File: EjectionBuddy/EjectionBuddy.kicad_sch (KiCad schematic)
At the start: 19 parts, among them J2 Conn_01x08, SW1 SW_Push, SW2 SW_Push, U1 ESP32-S3-MINI-1

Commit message: More work on the side-mcu, ongoing
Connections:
- net EN: now reaches C7.1, R21.2, SW1.2, U1.45 (EN)
- net 0: now reaches C9.1, SW2.2, U1.4 (IO0)
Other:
- sheet connector renamed connecter
- added sheet side_mcu (side_mcu.kicad_sch)
- sheet connecter: file connector.kicad_sch -> connecter.kicad_sch
- note added: "MCUs"
- note removed: "MCU"
- moved on the sheet: C1, C2, C7, C9, D10, D12, D13, D14, D15, R21, R22, R23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

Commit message: Finished! QR and instruction pending
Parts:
- removed C1: 10u, Capacitor_SMD:C_0603_1608Metric, symbol Device:C
- removed C2, C7, C9: 0.1u, Capacitor_SMD:C_0603_1608Metric, symbol Device:C
- removed D10, D12, D13, D14, D15: LED, symbol Device:LED
- removed J2: Conn_01x08, symbol Connector_Generic:Conn_01x08
- removed R21: 10k, Resistor_SMD:R_0603_1608Metric, symbol Device:R
- removed R22, R23, R24: 39k, symbol Device:R
- removed R26: 1k, symbol Device:R
- removed R27: 2.7k, symbol Device:R
- removed SW1, SW2: SW_Push, Button_Switch_SMD:SW_SPST_PTS810, symbol Switch:SW_Push
- removed U1: ESP32-S3-MINI-1, RF_Module:ESP32-S2-MINI-1, symbol RF_Module:ESP32-S3-MINI-1
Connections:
- no-connect marks 16 -> 0
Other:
- sheet sense renamed power_sense
- added sheet baro (baro.kicad_sch)
- added sheet detach_sense (detach_sense.kicad_sch)
- added sheet imu (imu.kicad_sch)
- added sheet led (led.kicad_sch)
- added sheet main_mcu (main_mcu.kicad_sch)
- added sheet stamp (stamp.kicad_sch)
- sheet connecter ports: added SM{SERIAL}, SM{SWD}; removed none
- sheet power_sense: file sense.kicad_sch -> power_sense.kicad_sch
- sheet side_mcu ports: added ONEWIRE, {SERIAL}, {SWD}; removed none
- sheet usb ports: added {USB}; removed D+, D-
- note added: "2025/4/3 - 4/13"
- note added: "SW_VBATOUT pull low to cut SW_PWRCUT pull high to cut"
- note added: "Sensors"
- note added: "v0.1"
- note removed: "0, 3, 45, 46 are strapping pins. 47, 48 work at 1.8V."
- note removed: "2025/4/3"
- note removed: "Breakouts in pads"
- note removed: "Green"
- note removed: "MCU module"
- note removed: "Red"

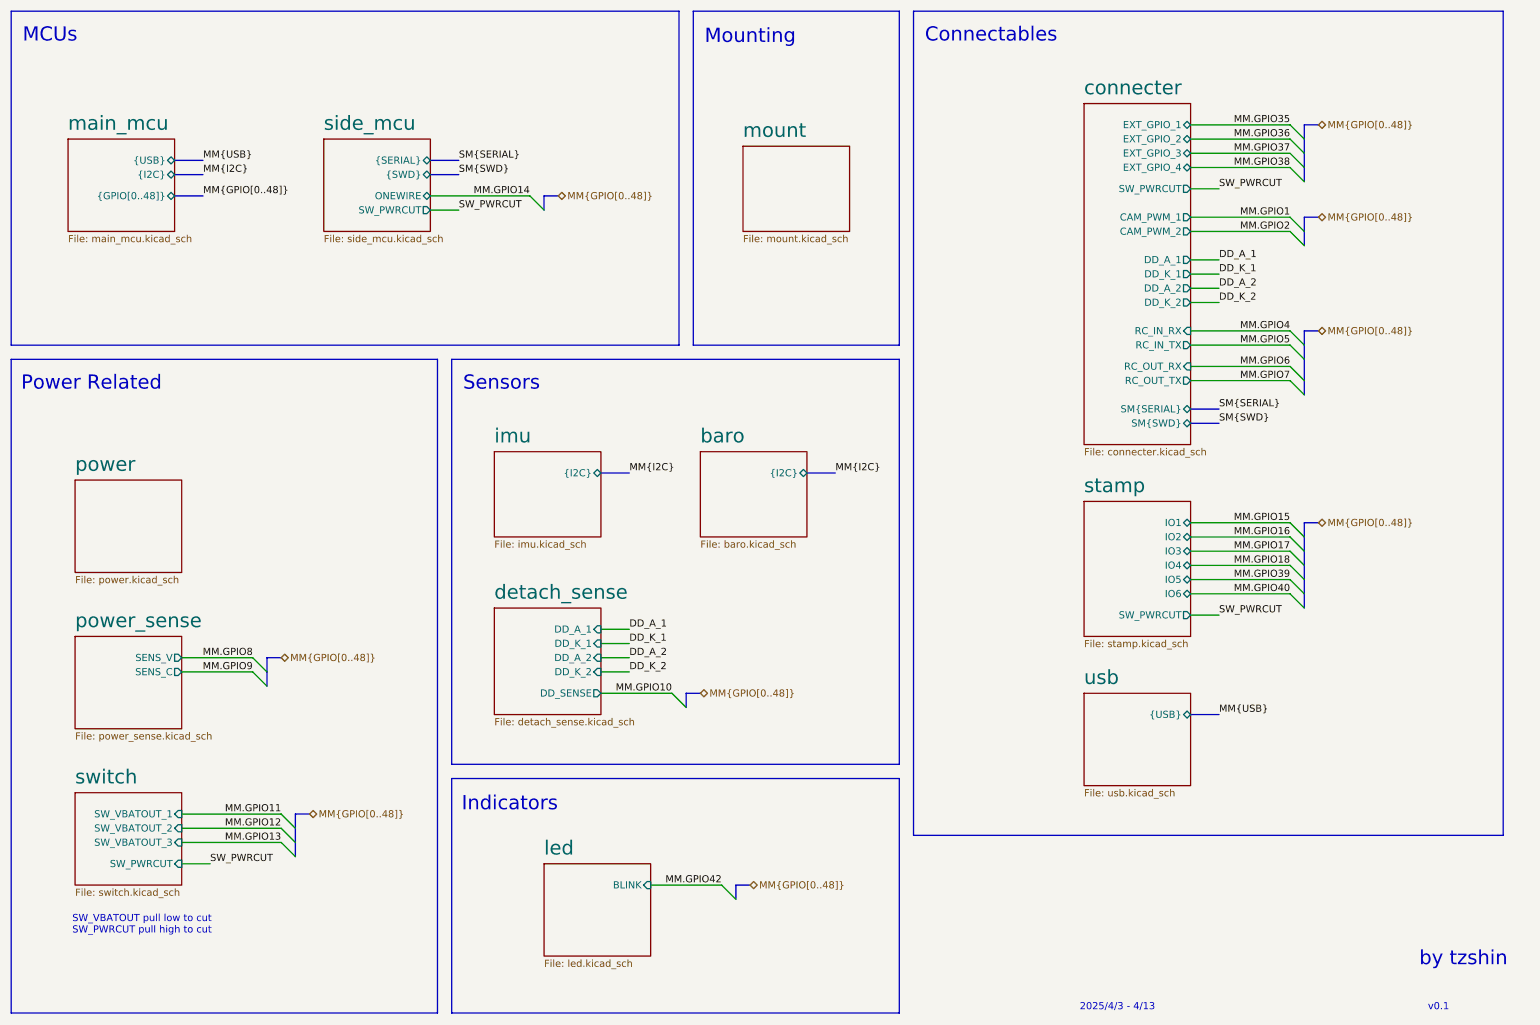
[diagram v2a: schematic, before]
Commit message: Side-mcu stm -> attiny, with improvements here and there
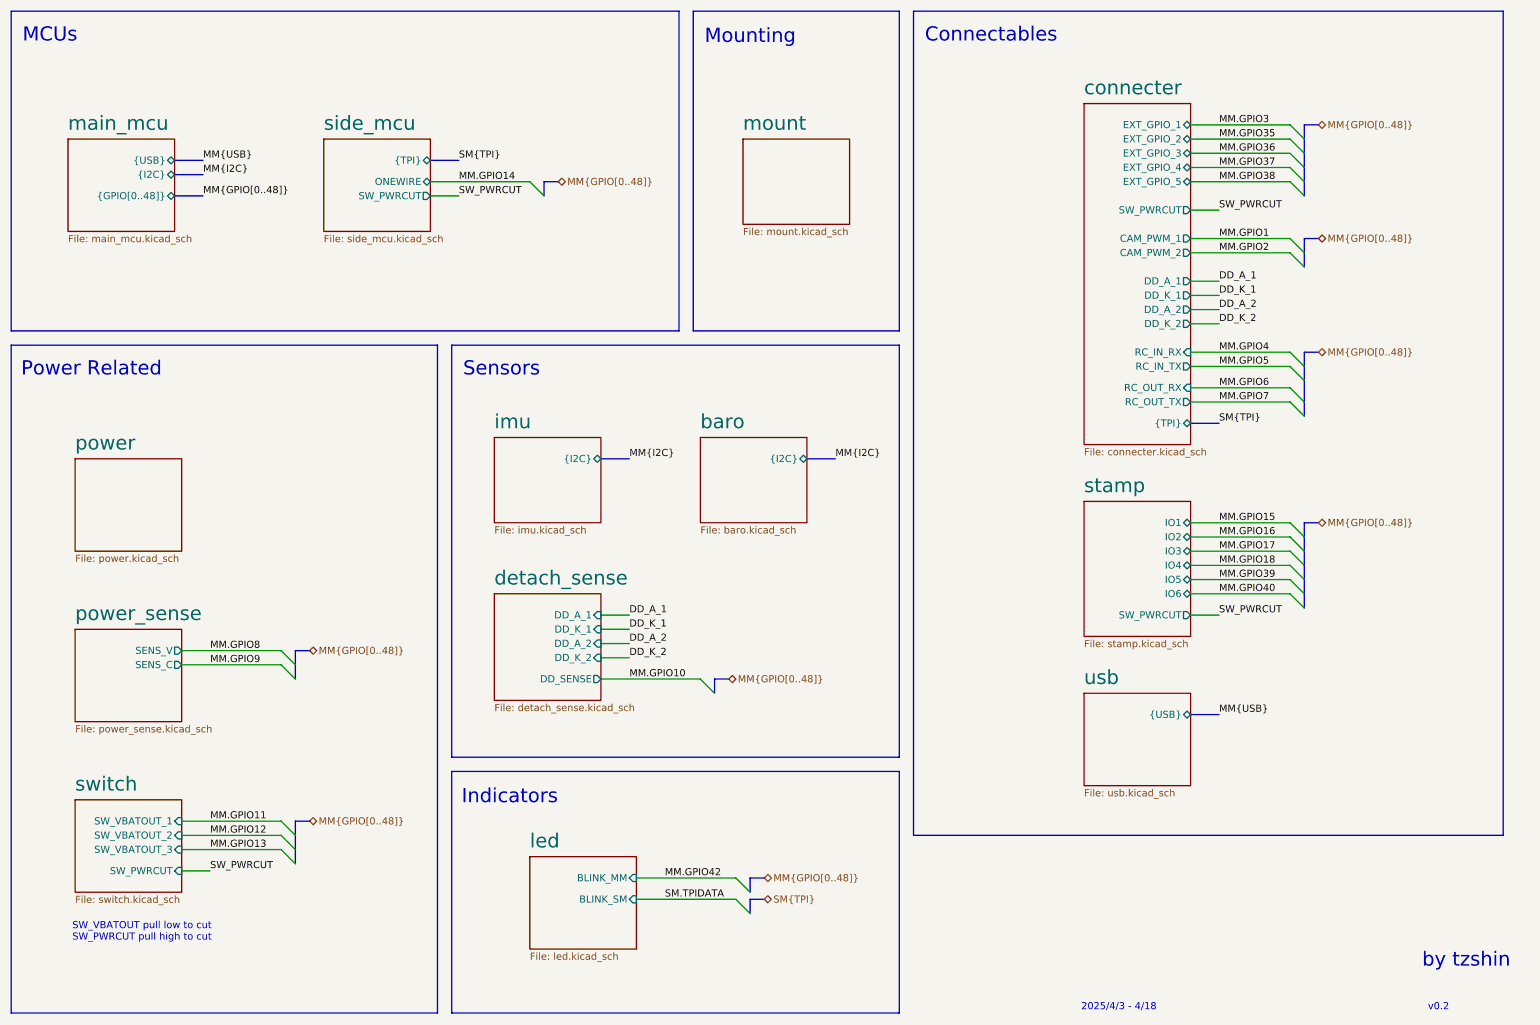
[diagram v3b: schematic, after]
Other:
- sheet connecter ports: added EXT_GPIO_5, {TPI}; removed SM{SERIAL}, SM{SWD}
- sheet led ports: added BLINK_MM, BLINK_SM; removed BLINK
- sheet side_mcu ports: added {TPI}; removed {SERIAL}, {SWD}
- note added: "2025/4/3 - 4/18"
- note added: "v0.2"
- note removed: "2025/4/3 - 4/13"
- note removed: "v0.1"

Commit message: Prodection version hw1.0 finished, with tidy-ups and bug-fixes
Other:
- note added: "v0.2.1"
- note removed: "v0.2"
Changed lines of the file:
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@@
 		)
 	)
-	(text "v0.2"
+	(text "v0.2.1"
 		(exclude_from_sim no)
 		(at 268.478 193.294 0)
@@
 	)
 	(bus_entry
-		(at 147.32 176.53)
+		(at 147.32 177.8)
 		(size -2.54 -2.54)
 		(stroke
@@
 	)
 	(bus_entry
-		(at 147.32 172.72)
+		(at 147.32 173.99)
 		(size -2.54 -2.54)
 		(stroke
@@
 	(bus
 		(pts
-			(xy 147.32 173.99) (xy 149.86 173.99)
+			(xy 147.32 175.26) (xy 149.86 175.26)
 		)
 		(stroke
@@
 	(wire
 		(pts
-			(xy 127 170.18) (xy 144.78 170.18)
+			(xy 127 171.45) (xy 144.78 171.45)
 		)
 		(stroke
@@
 	(bus
 		(pts
-			(xy 147.32 173.99) (xy 147.32 176.53)
+			(xy 147.32 175.26) (xy 147.32 177.8)
 		)
 		(stroke
@@
 	(bus
 		(pts
-			(xy 147.32 170.18) (xy 147.32 172.72)
+			(xy 147.32 171.45) (xy 147.32 173.99)
 		)
 		(stroke
@@
 	(wire
 		(pts
-			(xy 127 173.99) (xy 144.78 173.99)
+			(xy 127 175.26) (xy 144.78 175.26)
 		)
 		(stroke
@@
 	(bus
 		(pts
-			(xy 147.32 170.18) (xy 149.86 170.18)
+			(xy 147.32 171.45) (xy 149.86 171.45)
 		)
 		(stroke
@@
 	)
 	(label "MM.GPIO42"
-		(at 132.08 170.18 0)
+		(at 132.08 171.45 0)
 		(effects
 			(font
@@
 	)
 	(label "SM.TPIDATA"
-		(at 132.08 173.99 0)
+		(at 132.08 175.26 0)
 		(effects
 			(font
@@
 	(hierarchical_label "SM{TPI}"
 		(shape bidirectional)
-		(at 149.86 173.99 0)
+		(at 149.86 175.26 0)
 		(effects
 			(font
@@
 	(hierarchical_label "MM{GPIO[0..48]}"
 		(shape bidirectional)
-		(at 149.86 170.18 0)
+		(at 149.86 171.45 0)
 		(effects
 			(font
@@
 	)
 	(sheet
-		(at 107.95 166.37)
+		(at 107.95 167.64)
 		(size 19.05 16.51)
 		(exclude_from_sim no)
@@
 		)
 		(property "Sheetname" "led"
-			(at 107.95 165.0234 0)
+			(at 107.95 166.2934 0)
 			(effects
 				(font
@@
 		)
 		(property "Sheetfile" "led.kicad_sch"
-			(at 107.95 183.4646 0)
+			(at 107.95 184.7346 0)
 			(effects
 				(font
@@
 		)
 		(pin "BLINK_MM" input
-			(at 127 170.18 0)
+			(at 127 171.45 0)
 			(effects
 				(font
@@
 		)
 		(pin "BLINK_SM" input
-			(at 127 173.99 0)
-			(effects
-				(font
+			(at 127 175.26 0)
+			(effects
+				(font

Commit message: Untrack sch renaming poop and renamed connecter.sch to connector.sch
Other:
- sheet connecter renamed connector
- sheet connector: file connecter.kicad_sch -> connector.kicad_sch
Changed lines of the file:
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@@
 			(color 0 0 0 0.0000)
 		)
-		(property "Sheetname" "connecter"
+		(property "Sheetname" "connector"
 			(at 207.01 30.4034 0)
 			(effects
@@
 			)
 		)
-		(property "Sheetfile" "connecter.kicad_sch"
+		(property "Sheetfile" "connector.kicad_sch"
 			(at 207.01 93.2946 0)
 			(effects

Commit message: Fixed a FATAL imu wiring fault, CPOUT
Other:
- note added: "v0.2.2"
- note removed: "v0.2.1"
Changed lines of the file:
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@@
 		)
 	)
-	(text "v0.2.1"
+	(text "v0.2.2"
 		(exclude_from_sim no)
 		(at 268.478 193.294 0)
